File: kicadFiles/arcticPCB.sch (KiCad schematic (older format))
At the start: 175 parts, among them J1 TYPE-C-31-M12_13, J2 Conn_01x14, J3 Conn_ARM_JTAG_SWD_10, SW1 ESC, SW10 9, SW11 0, SW12 -_, SW13 +=, SW14 2U BKSP, SW15 TAB_150, SW16 Q, SW17 W, SW18 E, SW19 R, SW2 1, SW20 T, SW21 Y, SW22 U, SW23 I, SW24 O, SW25 P, SW26 [{, SW27 ]}, SW28 \\|_150, SW29 CAPS_175, SW3 2, SW30 A, SW31 S, SW32 D, SW33 F, SW34 G, SW35 H, SW36 J, SW37 K, SW38 L, SW39 :;, SW4 3, SW40 \"', SW41 ENTER_225, SW42 LSHIFT_225, SW43 Z, SW44 X, SW45 C, SW46 V, SW47 B, SW48 N, SW49 M, SW5 4, SW50 <,, SW51 >., SW52 ?/, SW53 RSHIFT_275, SW54 LCTRL_150, SW55 LGUI_100, SW56 LALT_150, SW57 SPACE_7U, SW58 RALT_150, SW59 RGUI_100, SW6 5, SW60 RCTRL_150, SW61 FN_100, SW62 RSHIFT_175, SW63 STEPPED_CAPS_125, SW64 1U LBKSP, SW65 1U RBKSP, SW7 6, SW8 7, SW9 8, U1 STM32F072-LQFP48, U2 USBLC6-2SC6, U3 MCP1700-3302E_SOT23

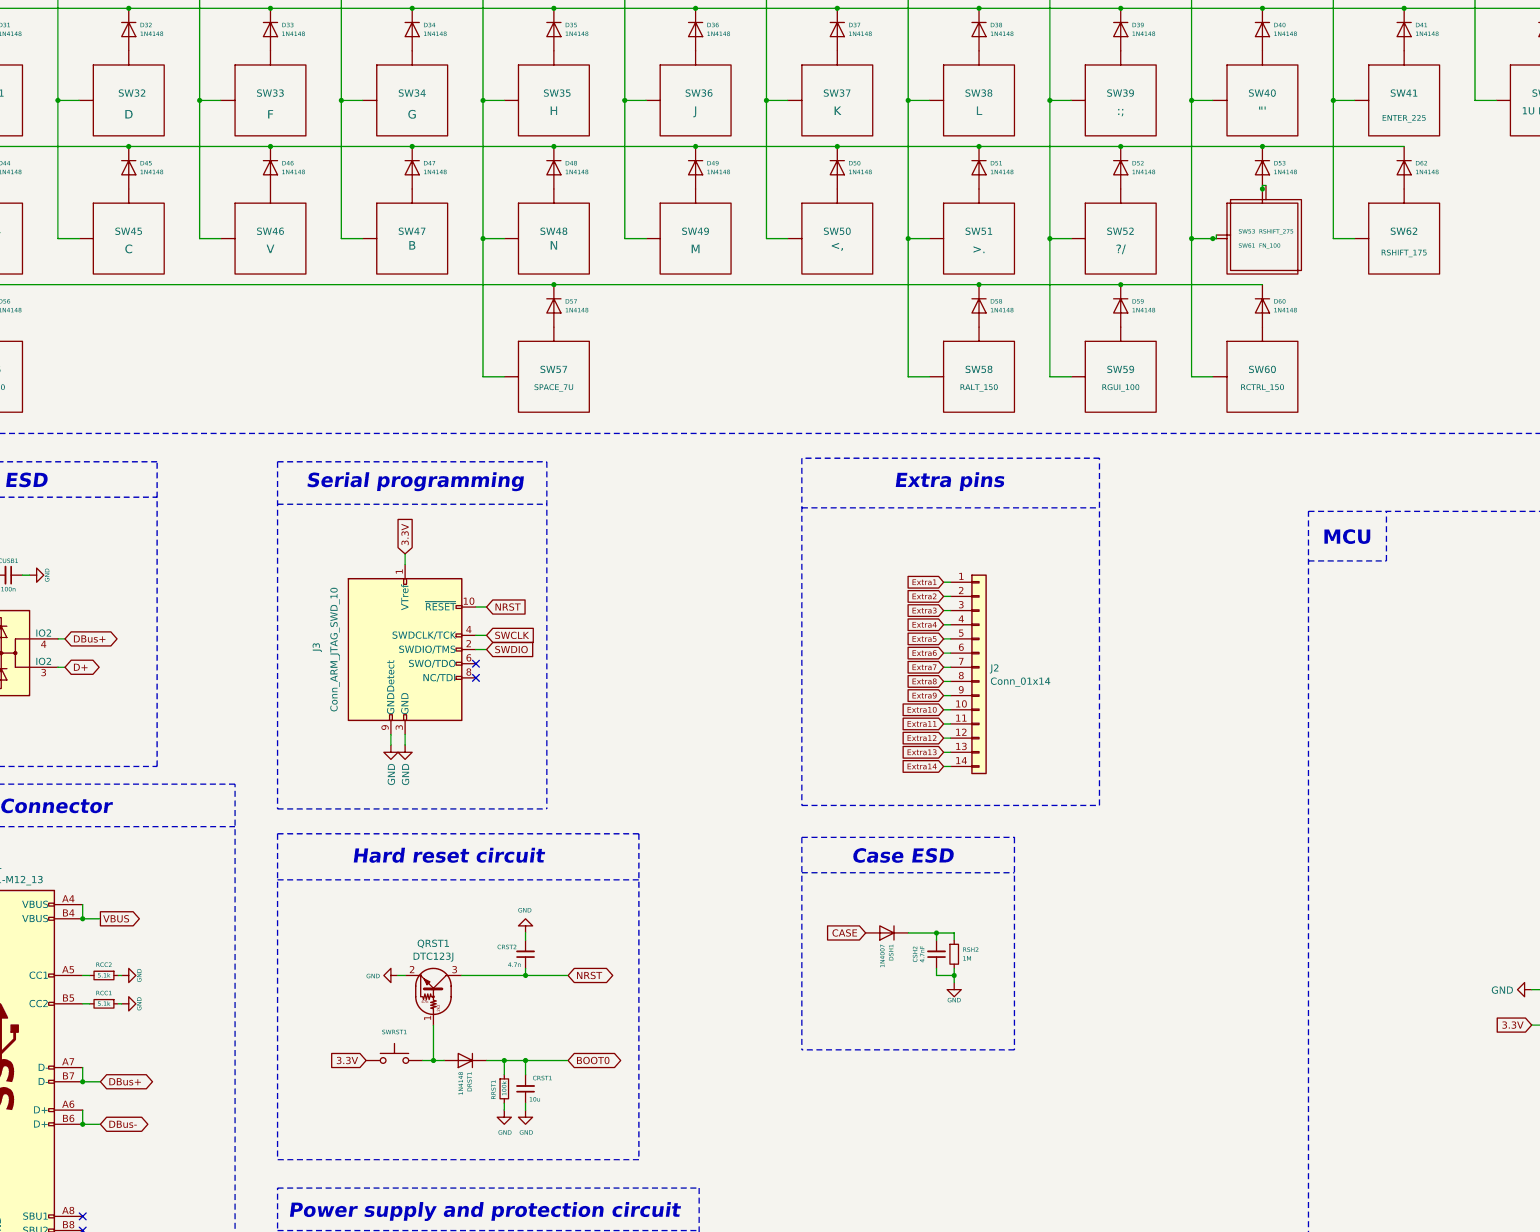
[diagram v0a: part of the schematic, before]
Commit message: Solve pre-Alpha prototype issues
This commit solves the issues found in the pre-Alpha prototypes:

- In the USB connector, the D+ and D- pads were switched; this has been fixed and the differential pair routing was improved;
- The split Right Shift keyswitches SW62 for the 1.75U RShift and 1U SW61 for the Fn were in the wrong orientation: the Fn key SW61 was on the left and SW62 was on the left. They were swapped for the right orientation now;
- Also, to make firmware definitions easier, the 1.75U RShift key and 2.75U RShift key are now at the same position, whereas in pre-Alpha SW62 for the 1.75RShift was at the same position with SW61 for the 1U Fn, which made firmware need two definitions. This has now been fixed.
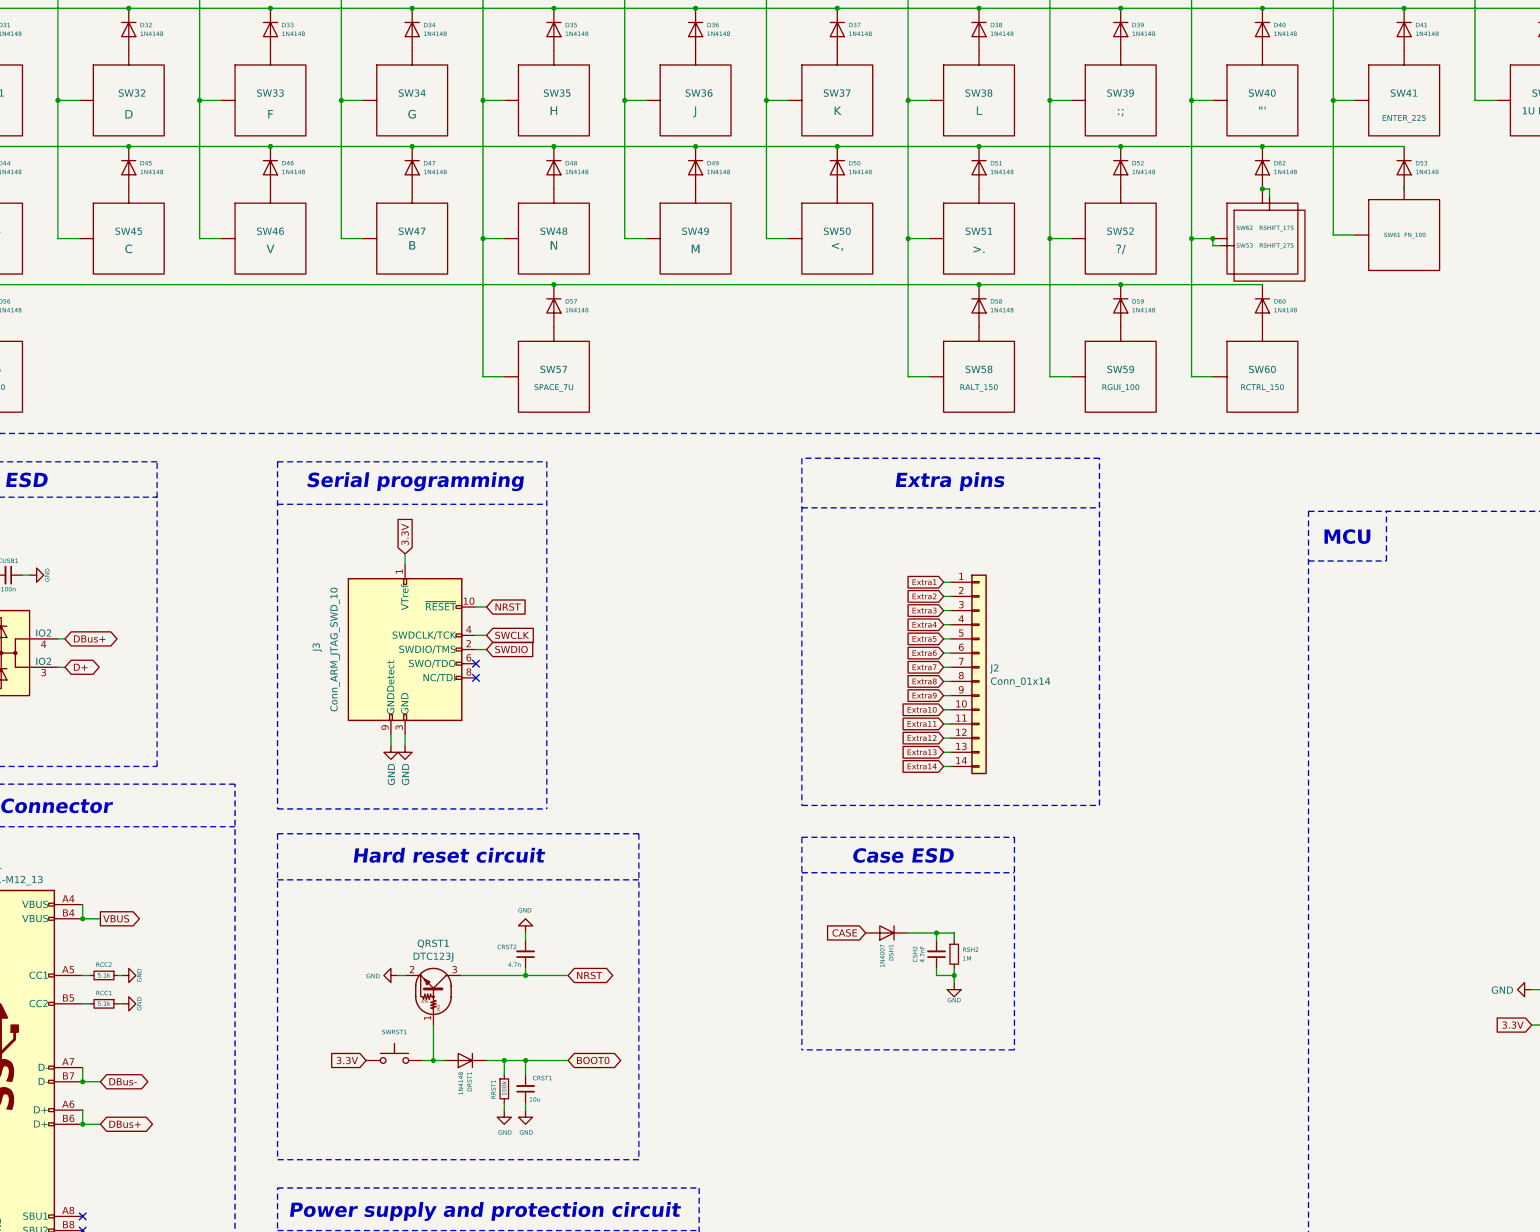
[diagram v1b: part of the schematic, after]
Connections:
- net Col12: now also SW62.1 (Col); no longer SW61.1 (Col)
- net Col13: now also SW61.1 (Col); no longer SW62.1 (Col)
- net DBus+: now also J1.A6 (D+), J1.B6 (D+); no longer J1.A7 (D-), J1.B7 (D-)
- net DBus-: now also J1.A7 (D-), J1.B7 (D-); no longer J1.A6 (D+), J1.B6 (D+)
- net at D53.2 (A), SW61.2 (Row): no longer SW53.2 (Row)
- net at D62.2 (A), SW62.2 (Row): now also SW53.2 (Row)
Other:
- moved on the sheet: D53, D62, SW53, SW61, SW62

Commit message: Updated files and README
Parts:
- added L6: Putain Logo, arcticGraphics:putainLogo_50_5, symbol Mechanical:MountingHole
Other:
- moved on the sheet: H1, H10, H2, H3, H4, H5, H6, H7, H8, H9
